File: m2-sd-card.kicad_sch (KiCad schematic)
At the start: 20 parts, among them J1 M.2_Key_E, J2 Micro_SD_Card_Det2, U1 AP2120N-1.8, U2 NVT4857UK

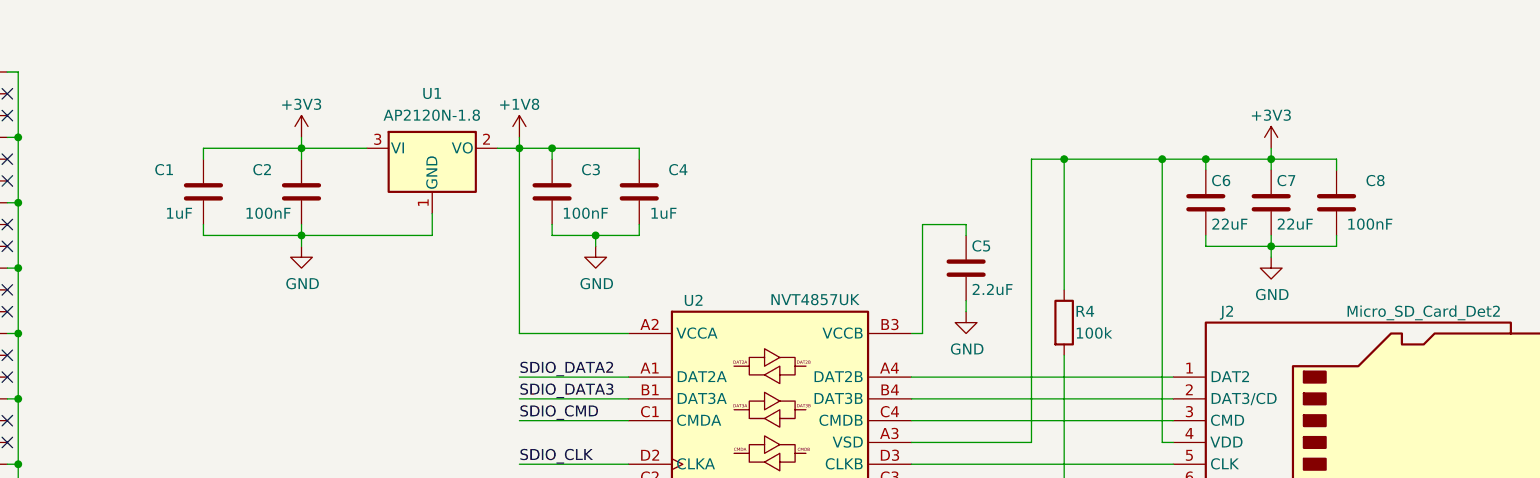
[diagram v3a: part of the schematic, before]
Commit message: Finish the routing of the board and export the gerbers and all manufacturing files
Add fab notes to the layout.

Generate a fabrication drawing and include it in the gerbers directory
since that is the location PCBWay will use (when this directory's
contents are archived into a zip).

Export the 3D step model of the board.

Export the IPC-D-356 netlist file which will be used to verify the
gerbers.
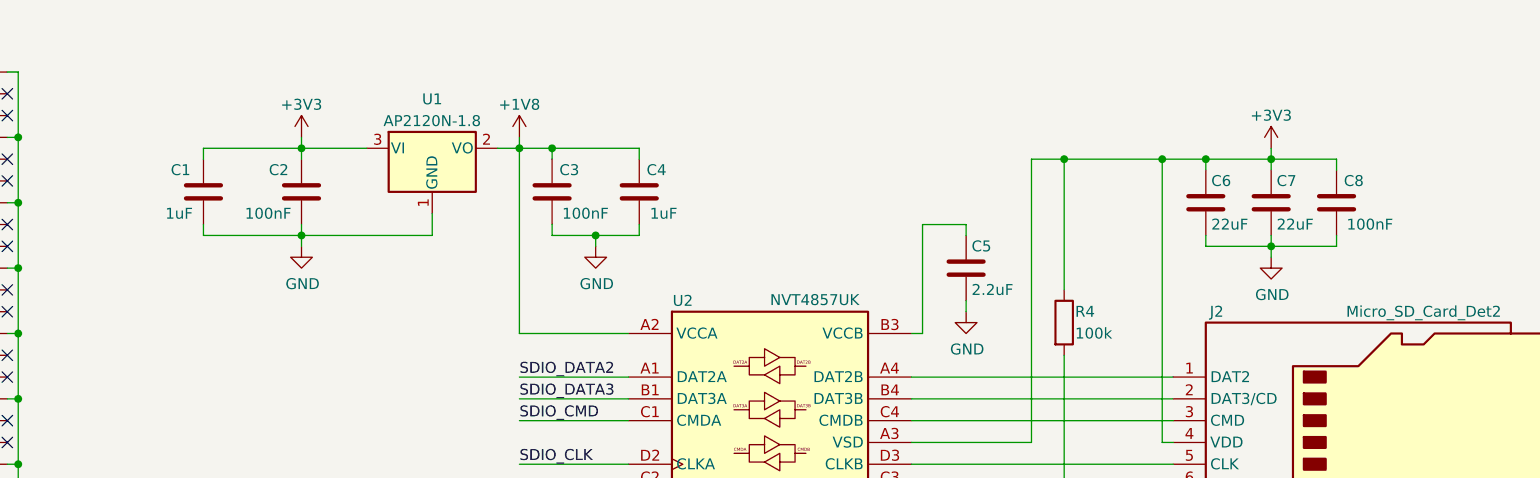
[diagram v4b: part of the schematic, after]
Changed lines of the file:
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@@
   (title_block
     (title "M.2 SD Card")
-    (date "2023-05-09")
+    (date "2023-05-11")
     (rev "v0.5.0")
     (company "Purism SPC")
@@
   (symbol (lib_id "Device:C") (at 116.84 64.77 0) (mirror y) (unit 1)
     (in_bom yes) (on_board yes) (dnp no)
-    (property "Reference" "C2" (at 111.125 62.23 0)
+    (property "Reference" "C2" (at 113.03 62.23 0)
       (effects (font (size 1.27 1.27)) (justify right))
     )
@@
   (symbol (lib_id "Device:C") (at 105.41 64.77 0) (mirror y) (unit 1)
     (in_bom yes) (on_board yes) (dnp no)
-    (property "Reference" "C1" (at 99.695 62.23 0)
+    (property "Reference" "C1" (at 101.6 62.23 0)
       (effects (font (size 1.27 1.27)) (justify right))
     )
@@
   (symbol (lib_id "Device:C") (at 146.05 64.77 0) (unit 1)
     (in_bom yes) (on_board yes) (dnp no)
-    (property "Reference" "C3" (at 151.765 62.23 0)
+    (property "Reference" "C3" (at 149.225 62.23 0)
       (effects (font (size 1.27 1.27)) (justify right))
     )
@@
   (symbol (lib_id "m2-sd-card:NVT4857UK") (at 171.45 97.79 0) (unit 1)
     (in_bom yes) (on_board yes) (dnp no)
-    (property "Reference" "U2" (at 162.56 77.47 0)
+    (property "Reference" "U2" (at 161.29 77.47 0)
       (effects (font (size 1.27 1.27)))
     )
@@
   (symbol (lib_id "Device:C") (at 156.21 64.77 0) (unit 1)
     (in_bom yes) (on_board yes) (dnp no)
-    (property "Reference" "C4" (at 161.925 62.23 0)
+    (property "Reference" "C4" (at 159.385 62.23 0)
       (effects (font (size 1.27 1.27)) (justify right))
     )
@@
   (symbol (lib_id "Connector:Micro_SD_Card_Det2") (at 241.3 96.52 0) (unit 1)
     (in_bom yes) (on_board yes) (dnp no)
-    (property "Reference" "J2" (at 224.79 78.74 0)
+    (property "Reference" "J2" (at 223.52 78.74 0)
       (effects (font (size 1.27 1.27)))
     )
@@
   (symbol (lib_id "Device:C") (at 237.49 66.04 0) (unit 1)
     (in_bom yes) (on_board yes) (dnp no)
-    (property "Reference" "C8" (at 243.205 63.5 0)
+    (property "Reference" "C8" (at 240.665 63.5 0)
       (effects (font (size 1.27 1.27)) (justify right))
     )
@@
   )
   (symbol (lib_id "m2-sd-card:AP2120N-1.8") (at 132.08 59.69 0) (unit 1)
-    (in_bom yes) (on_board yes) (dnp no) (fields_autoplaced)
-    (property "Reference" "U1" (at 132.08 53.34 0)
-      (effects (font (size 1.27 1.27)))
-    )
-    (property "Value" "AP2120N-1.8" (at 132.08 55.88 0)
-      (effects (font (size 1.27 1.27)))
-    )
+    (in_bom yes) (on_board yes) (dnp no)
+    (property "Reference" "U1" (at 132.08 53.975 0)
+      (effects (font (size 1.27 1.27)))
+    )
+    (property "Value" "AP2120N-1.8" (at 132.08 56.515 0)
+      (effects (font (size 1.27 1.27)))
+    )
